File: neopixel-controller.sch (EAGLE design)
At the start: 12 parts, among them J1 Power, U1 ATTiny85

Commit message: Final revision
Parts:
- added C2: 0.1uF, resistor:C-USC0805
- C1: value 1mF -> 1000uF; device SparkFun-Capacitors:1000UF-RADIAL-5MM-25V-20% -> JoshCustom:CAPACITOR
- LED1, LED2: device JoshCustom:NEOPIXEL -> JoshCustom:NEOPIXEL0.100_PINHEAD
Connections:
- net GND: now also C1.NEGATIVE, C2.2; no longer C1.-
- net VCC: now also C1.POSITIVE, C2.1; no longer C1.+

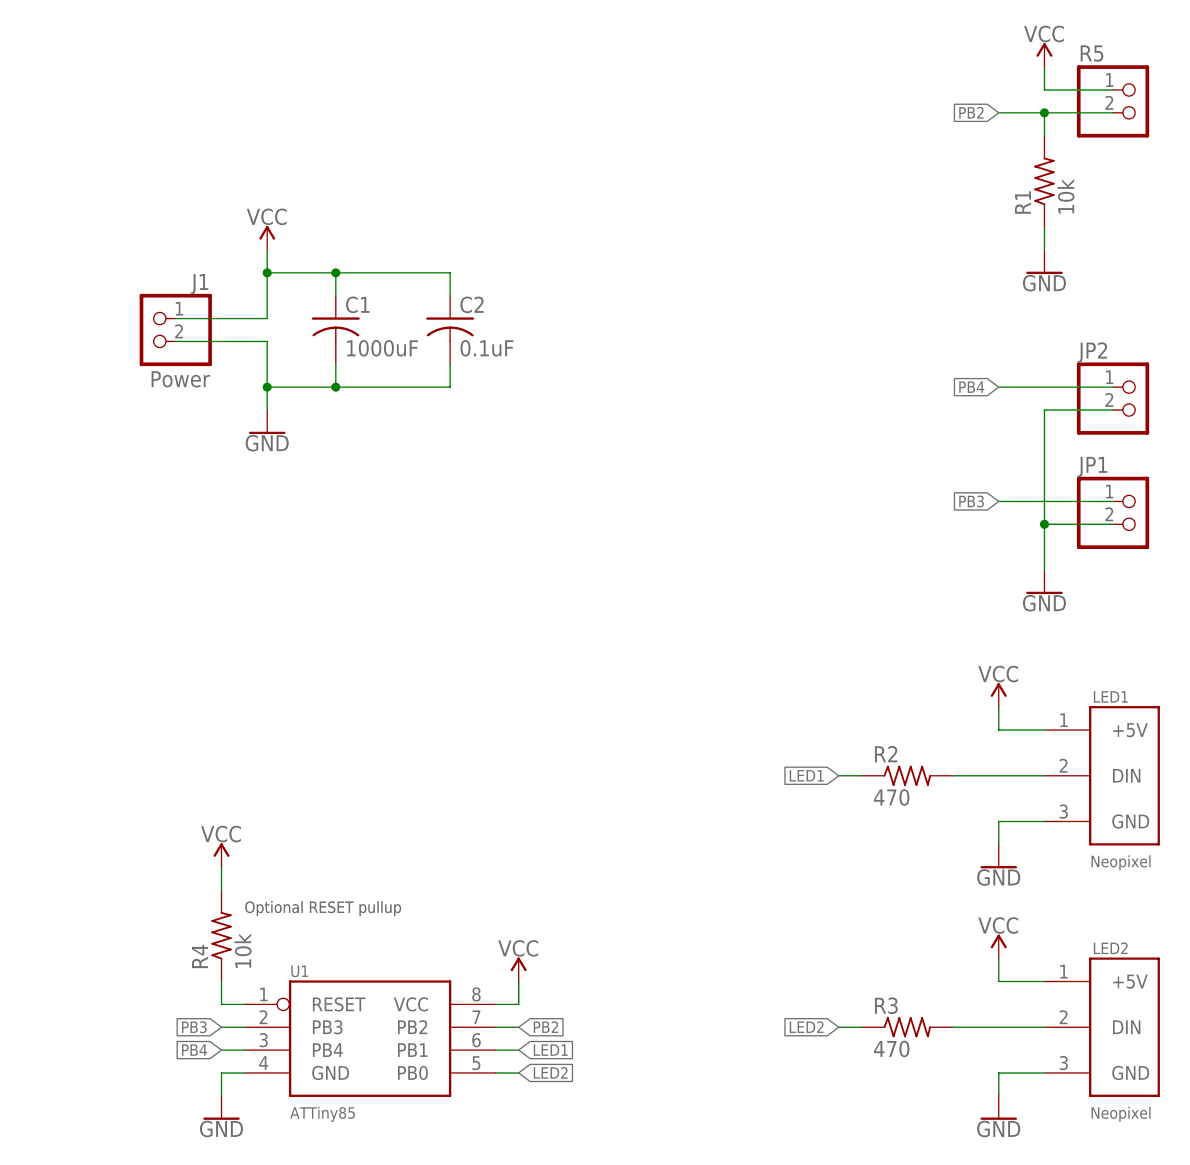
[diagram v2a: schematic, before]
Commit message: Initial swap of Neopixel controller to SOIC ATTiny85
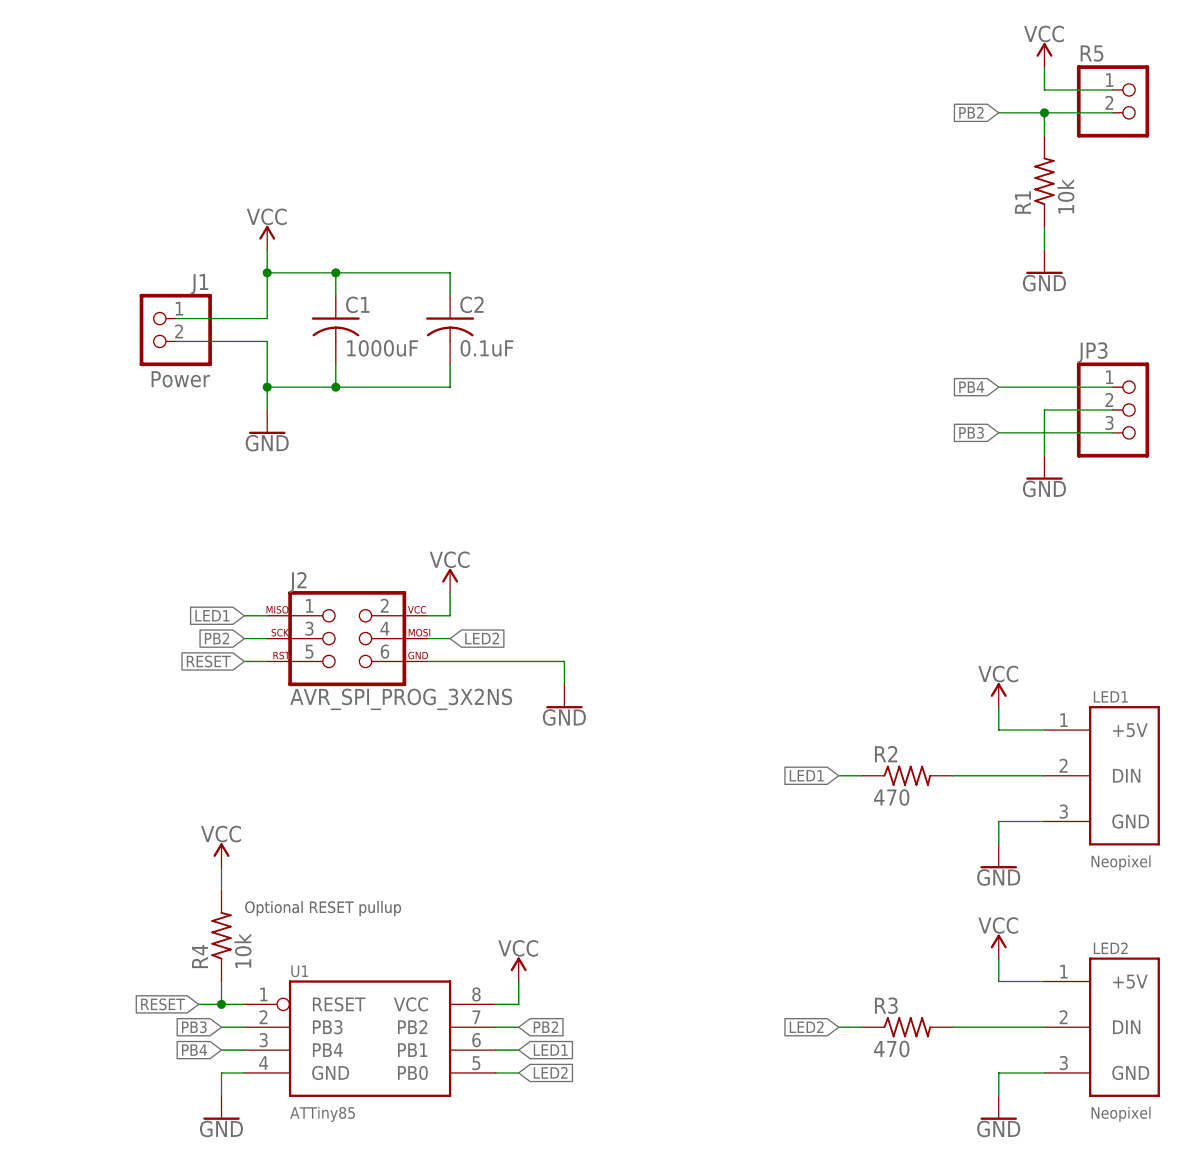
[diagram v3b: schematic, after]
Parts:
- removed JP1, JP2: (no value), pinhead:PINHD-1X2
- added J2: AVR_SPI_PROG_3X2NS, SparkFun-Connectors:AVR_SPI_PROG_3X2NS
- added JP3: (no value), pinhead:PINHD-1X3
- U1: device JoshCustom:ATTINY85PDIP8_SOCKET -> JoshCustom:ATTINY85SOIC8
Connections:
- removed net N$5: R4.1, U1.RESET
- new net RESET: J2.5, R4.1, U1.RESET
- net GND: now also J2.6, JP3.2; no longer JP1.2, JP2.2
- net LED1: now also J2.1
- net LED2: now also J2.4
- net PB2: now also J2.3
- net PB3: now also JP3.3; no longer JP1.1
- net PB4: now also JP3.1; no longer JP2.1
- net VCC: now also J2.2
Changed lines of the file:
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@@
 <drawing>
 <settings>
-<setting alwaysvectorfont="no"/>
+<setting alwaysvectorfont="yes"/>
 <setting verticaltext="up"/>
 </settings>
@@
 <parts>
 <part name="J1" library="pinhead" library_urn="urn:adsk.eagle:library:325" deviceset="PINHD-1X2" device="" package3d_urn="urn:adsk.eagle:package:22435/2" value="Power"/>
-<part name="U1" library="JoshCustom" deviceset="ATTINY85" device="PDIP8_SOCKET" value="ATTiny85"/>
+<part name="U1" library="JoshCustom" deviceset="ATTINY85" device="SOIC8" value="ATTiny85"/>
 <part name="LED1" library="JoshCustom" deviceset="NEOPIXEL" device="0.100_PINHEAD" value="Neopixel"/>
 <part name="LED2" library="JoshCustom" deviceset="NEOPIXEL" device="0.100_PINHEAD" value="Neopixel"/>
 <part name="R5" library="pinhead" library_urn="urn:adsk.eagle:library:325" deviceset="PINHD-1X2" device="" package3d_urn="urn:adsk.eagle:package:22435/2"/>
-<part name="JP1" library="pinhead" library_urn="urn:adsk.eagle:library:325" deviceset="PINHD-1X2" device="" package3d_urn="urn:adsk.eagle:package:22435/2"/>
 <part name="R1" library="resistor" library_urn="urn:adsk.eagle:library:348" deviceset="R-US_" device="R0805" package3d_urn="urn:adsk.eagle:package:26059/1" value="10k"/>
 <part name="R2" library="resistor" library_urn="urn:adsk.eagle:library:348" deviceset="R-US_" device="R0805" package3d_urn="urn:adsk.eagle:package:26059/1" value="470"/>
 <part name="R3" library="resistor" library_urn="urn:adsk.eagle:library:348" deviceset="R-US_" device="R0805" package3d_urn="urn:adsk.eagle:package:26059/1" value="470"/>
 <part name="R4" library="resistor" library_urn="urn:adsk.eagle:library:348" deviceset="R-US_" device="R0805" package3d_urn="urn:adsk.eagle:package:26059/1" value="10k"/>
-<part name="JP2" library="pinhead" library_urn="urn:adsk.eagle:library:325" deviceset="PINHD-1X2" device="" package3d_urn="urn:adsk.eagle:package:22435/2"/>
 <part name="SUPPLY1" library="SparkFun-PowerSymbols" deviceset="VCC" device=""/>
 <part name="SUPPLY2" library="SparkFun-PowerSymbols" deviceset="VCC" device=""/>
@@
 <part name="C2" library="resistor" library_urn="urn:adsk.eagle:library:348" deviceset="C-US" device="C0805" package3d_urn="urn:adsk.eagle:package:23617/2" value="0.1uF"/>
 <part name="C1" library="JoshCustom" deviceset="CAPACITOR" device="" value="1000uF"/>
+<part name="J2" library="SparkFun-Connectors" deviceset="AVR_SPI_PROG_3X2" device="NS"/>
+<part name="SUPPLY6" library="SparkFun-PowerSymbols" deviceset="VCC" device=""/>
+<part name="GND7" library="SparkFun-PowerSymbols" deviceset="GND" device=""/>
+<part name="JP3" library="pinhead" library_urn="urn:adsk.eagle:library:325" deviceset="PINHD-1X3" device="" package3d_urn="urn:adsk.eagle:package:22458/2"/>
 </parts>
 <sheets>
@@
 <attribute name="VALUE" x="107.95" y="109.22" size="1.778" layer="96"/>
 </instance>
-<instance part="JP1" gate="G$1" x="114.3" y="68.58" smashed="yes">
-<attribute name="NAME" x="107.95" y="74.295" size="1.778" layer="95"/>
-<attribute name="VALUE" x="107.95" y="63.5" size="1.778" layer="96"/>
-</instance>
 <instance part="R1" gate="G$1" x="104.14" y="106.68" smashed="yes" rot="R90">
 <attribute name="NAME" x="102.6414" y="102.87" size="1.778" layer="95" rot="R90"/>
@@
 <attribute name="VALUE" x="16.002" y="19.05" size="1.778" layer="96" rot="R90"/>
 </instance>
-<instance part="JP2" gate="G$1" x="114.3" y="81.28" smashed="yes">
-<attribute name="NAME" x="107.95" y="86.995" size="1.778" layer="95"/>
-<attribute name="VALUE" x="107.95" y="76.2" size="1.778" layer="96"/>
-</instance>
 <instance part="SUPPLY1" gate="G$1" x="17.78" y="99.06" smashed="yes">
 <attribute name="VALUE" x="17.78" y="101.854" size="1.778" layer="96" align="bottom-center"/>
@@
 <attribute name="VALUE" x="12.7" y="33.274" size="1.778" layer="96" align="bottom-center"/>
 </instance>
-<instance part="GND5" gate="1" x="104.14" y="60.96" smashed="yes">
-<attribute name="VALUE" x="104.14" y="60.706" size="1.778" layer="96" align="top-center"/>
+<instance part="GND5" gate="1" x="104.14" y="73.66" smashed="yes">
+<attribute name="VALUE" x="104.14" y="73.406" size="1.778" layer="96" align="top-center"/>
 </instance>
 <instance part="GND6" gate="1" x="104.14" y="96.52" smashed="yes">
@@
 <attribute name="NAME" x="26.416" y="92.075" size="1.778" layer="95"/>
 <attribute name="VALUE" x="26.416" y="87.249" size="1.778" layer="96"/>
+</instance>
+<instance part="J2" gate="G$1" x="25.4" y="55.88" smashed="yes">
+<attribute name="NAME" x="20.32" y="61.468" size="1.778" layer="95" font="vector"/>
+<attribute name="VALUE" x="20.32" y="48.514" size="1.778" layer="96" font="vector"/>
+</instance>
+<instance part="SUPPLY6" gate="G$1" x="38.1" y="60.96" smashed="yes">
+<attribute name="VALUE" x="38.1" y="63.754" size="1.778" layer="96" align="bottom-center"/>
+</instance>
+<instance part="GND7" gate="1" x="50.8" y="48.26" smashed="yes">
+<attribute name="VALUE" x="50.8" y="48.006" size="1.778" layer="96" align="top-center"/>
+</instance>
+<instance part="JP3" gate="A" x="114.3" y="81.28" smashed="yes">
+<attribute name="NAME" x="107.95" y="86.995" size="1.778" layer="95"/>
+<attribute name="VALUE" x="107.95" y="73.66" size="1.778" layer="96"/>
 </instance>
 </instances>
@@
 <wire x1="104.14" y1="116.84" x2="104.14" y2="119.38" width="0.1524" layer="91"/>
 </segment>
+<segment>
+<pinref part="J2" gate="G$1" pin="2"/>
+<pinref part="SUPPLY6" gate="G$1" pin="VCC"/>
+<wire x1="35.56" y1="58.42" x2="38.1" y2="58.42" width="0.1524" layer="91"/>
+<wire x1="38.1" y1="58.42" x2="38.1" y2="60.96" width="0.1524" layer="91"/>
+</segment>
 </net>
 <net name="GND" class="0">
@@
 </segment>
 <segment>
-<pinref part="JP2" gate="G$1" pin="2"/>
 <pinref part="GND5" gate="1" pin="GND"/>
 <wire x1="111.76" y1="81.28" x2="104.14" y2="81.28" width="0.1524" layer="91"/>
-<wire x1="104.14" y1="81.28" x2="104.14" y2="68.58" width="0.1524" layer="91"/>
-<pinref part="JP1" gate="G$1" pin="2"/>
-<wire x1="104.14" y1="68.58" x2="104.14" y2="63.5" width="0.1524" layer="91"/>
-<wire x1="111.76" y1="68.58" x2="104.14" y2="68.58" width="0.1524" layer="91"/>
-<junction x="104.14" y="68.58"/>
-</segment>
-</net>
-<net name="N$5" class="0">
-<segment>
-<pinref part="U1" gate="G$1" pin="RESET"/>
-<wire x1="15.24" y1="15.24" x2="12.7" y2="15.24" width="0.1524" layer="91"/>
-<pinref part="R4" gate="G$1" pin="1"/>
-<wire x1="12.7" y1="15.24" x2="12.7" y2="17.78" width="0.1524" layer="91"/>
+<wire x1="104.14" y1="81.28" x2="104.14" y2="76.2" width="0.1524" layer="91"/>
+<pinref part="JP3" gate="A" pin="2"/>
+</segment>
+<segment>
+<pinref part="J2" gate="G$1" pin="6"/>
+<wire x1="35.56" y1="53.34" x2="50.8" y2="53.34" width="0.1524" layer="91"/>
+<pinref part="GND7" gate="1" pin="GND"/>
+<wire x1="50.8" y1="53.34" x2="50.8" y2="50.8" width="0.1524" layer="91"/>
 </segment>
 </net>
@@
 </segment>
 <segment>
-<pinref part="JP1" gate="G$1" pin="1"/>
-<wire x1="111.76" y1="71.12" x2="99.06" y2="71.12" width="0.1524" layer="91"/>
-<label x="99.06" y="71.12" size="1.27" layer="95" rot="R180" xref="yes"/>
+<wire x1="111.76" y1="78.74" x2="99.06" y2="78.74" width="0.1524" layer="91"/>
+<label x="99.06" y="78.74" size="1.27" layer="95" rot="R180" xref="yes"/>
+<pinref part="JP3" gate="A" pin="3"/>
 </segment>
 </net>
@@
 </segment>
 <segment>
-<pinref part="JP2" gate="G$1" pin="1"/>
 <wire x1="111.76" y1="83.82" x2="99.06" y2="83.82" width="0.1524" layer="91"/>
 <label x="99.06" y="83.82" size="1.27" layer="95" rot="R180" xref="yes"/>
+<pinref part="JP3" gate="A" pin="1"/>
 </segment>
 </net>
@@
 <label x="99.06" y="114.3" size="1.27" layer="95" rot="R180" xref="yes"/>
 </segment>
+<segment>
+<pinref part="J2" gate="G$1" pin="3"/>
+<wire x1="17.78" y1="55.88" x2="15.24" y2="55.88" width="0.1524" layer="91"/>
+<label x="15.24" y="55.88" size="1.27" layer="95" rot="R180" xref="yes"/>
+</segment>
 </net>
 <net name="LED2" class="0">
@@
 <label x="81.28" y="12.7" size="1.27" layer="95" rot="R180" xref="yes"/>
 </segment>
+<segment>
+<pinref part="J2" gate="G$1" pin="4"/>
+<wire x1="35.56" y1="55.88" x2="38.1" y2="55.88" width="0.1524" layer="91"/>
+<label x="38.1" y="55.88" size="1.27" layer="95" xref="yes"/>
+</segment>
 </net>
 <net name="LED1" class="0">
@@
 <label x="81.28" y="40.64" size="1.27" layer="95" rot="R180" xref="yes"/>
 </segment>
-</net>
+<segment>
+<pinref part="J2" gate="G$1" pin="1"/>
+<wire x1="17.78" y1="58.42" x2="15.24" y2="58.42" width="0.1524" layer="91"/>
+<label x="15.24" y="58.42" size="1.27" layer="95" rot="R180" xref="yes"/>
+</segment>
+</net>
+<net name="RESET" class="0">
+<segment>
+<pinref part="J2" gate="G$1" pin="5"/>
+<wire x1="17.78" y1="53.34" x2="15.24" y2="53.34" width="0.1524" layer="91"/>
+<label x="15.24" y="53.34" size="1.27" layer="95" rot="R180" xref="yes"/>
+</segment>
+<segment>
+<pinref part="U1" gate="G$1" pin="RESET"/>
+<wire x1="15.24" y1="15.24" x2="12.7" y2="15.24" width="0.1524" layer="91"/>
+<label x="10.16" y="15.24" size="1.27" layer="95" rot="R180" xref="yes"/>
+<pinref part="R4" gate="G$1" pin="1"/>
+<wire x1="12.7" y1="15.24" x2="10.16" y2="15.24" width="0.1524" layer="91"/>
+<wire x1="12.7" y1="17.78" x2="12.7" y2="15.24" width="0.1524" layer="91"/>
+<junction x="12.7" y="15.24"/>
+</segment>
+</net>
